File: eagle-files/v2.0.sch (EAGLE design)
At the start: 32 parts, among them U2 MLX90614_

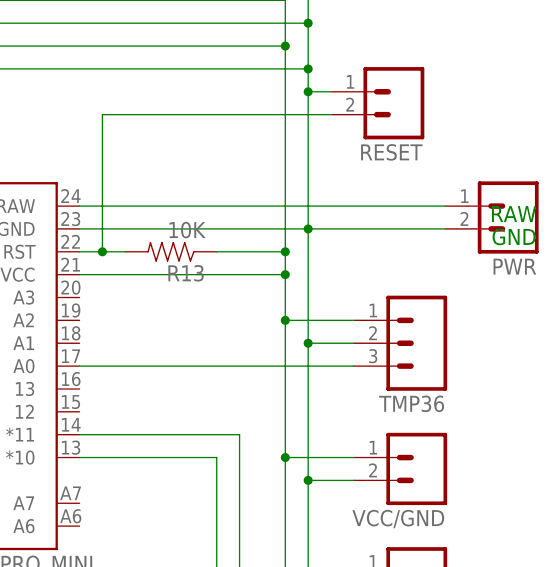
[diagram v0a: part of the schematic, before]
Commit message: Played with the eagle board and cleaned it up. Made clearances 12mil for everything.
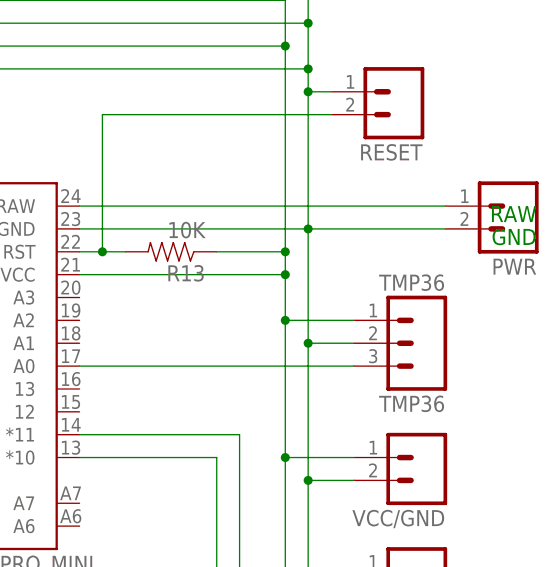
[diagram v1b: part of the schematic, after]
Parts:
- TMP36: value (none) -> TMP36
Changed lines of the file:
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@@
 <part name="RESET" library="SparkFun-Connectors" deviceset="M02" device="3.5MM_LOCK" value=""/>
 <part name="R13" library="SparkFun-Resistors" deviceset="10KOHM1/10W1%(0603)" device="0603" value="10K"/>
-<part name="TMP36" library="SparkFun-Connectors" deviceset="M03" device="SCREW_LOCK"/>
+<part name="TMP36" library="SparkFun-Connectors" deviceset="M03" device="SCREW_LOCK" value="TMP36"/>
 </parts>
 <sheets>
@@
 </sheet>
 </sheets>
-<errors>
-</errors>
 </schematic>
 </drawing>
